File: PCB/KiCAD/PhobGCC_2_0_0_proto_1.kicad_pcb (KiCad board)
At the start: 2 copper layers, 125.5 x 90.3 mm, 113 parts, among them J1 Conn_01x06_Female, J11 Conn_01x02, J14 Conn_01x06, J15 Conn_01x06, J2 Conn_01x02, J3 Conn_01x02, J4 Conn_01x01, J5 Rumble, J6 Conn_01x06, J8 USB_B_Micro, Q1 Q_NMOS_GSD, Q2 Q_PMOS_GDS, Q3 Q_NMOS_GSD, SW1 A, SW10 Dup, SW11 Dright, SW12 Ddown, SW2 B, SW3 X, SW4 Y, SW5 Start, SW6 L, SW7 R, SW8 Z, SW9 Dleft, U1 MCP3202, U10 DRV5055A3xDBZxQ1, U11 DRV5055A3xDBZxQ1, U12 USBLC6-2P6, U13 USBLC6-2P6, U2 Stickbox_Assembly_Main, U3 MCP3202, U4 DRV5055A3xDBZxQ1, U5 Stickbox_Assembly_CStick, U6 AMS1117-3.3, U7 W25Q128JVS, U8 RP2040, U9 DRV5055A3xDBZxQ1, Y1 Crystal_GND24

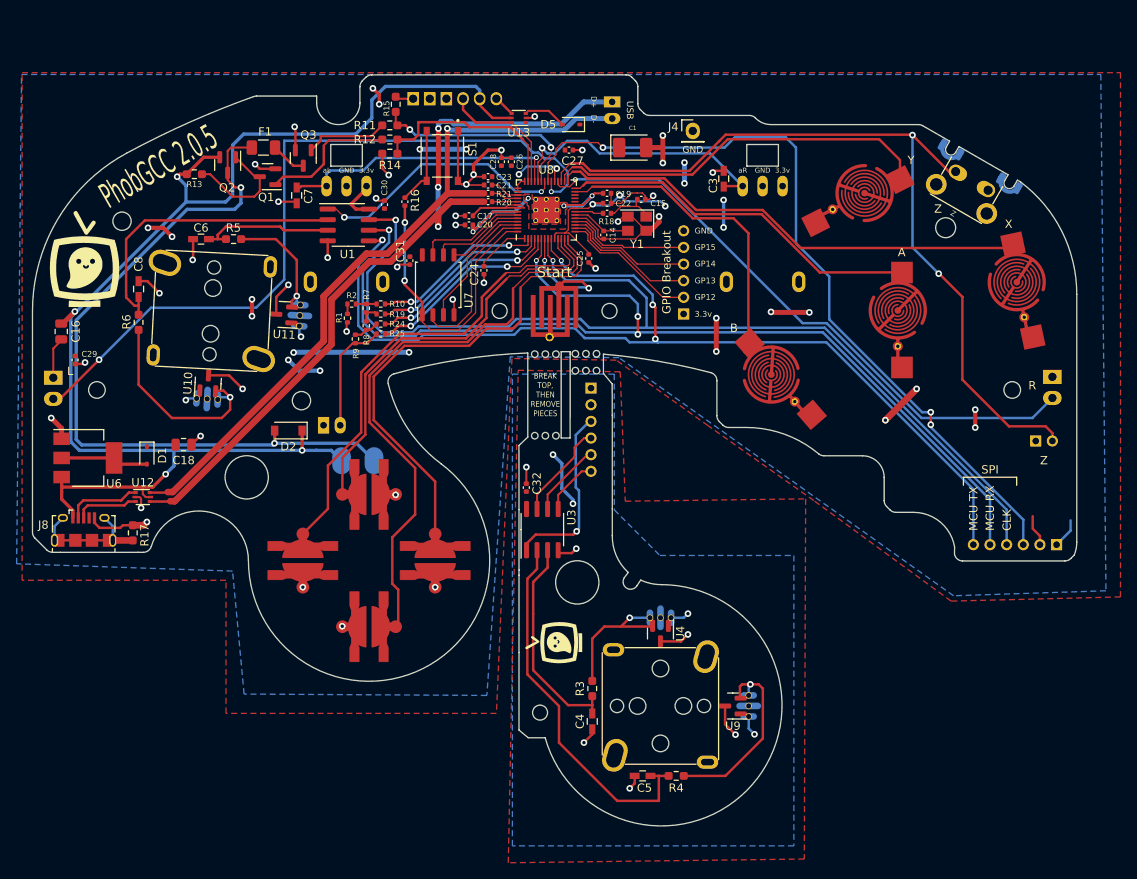
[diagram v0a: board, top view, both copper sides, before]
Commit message: NaxGCC Changes:
- update to KiCad 8
- replace micro USB & GCC connector with USB C
- add some JLCPCB symbols, footprints & models
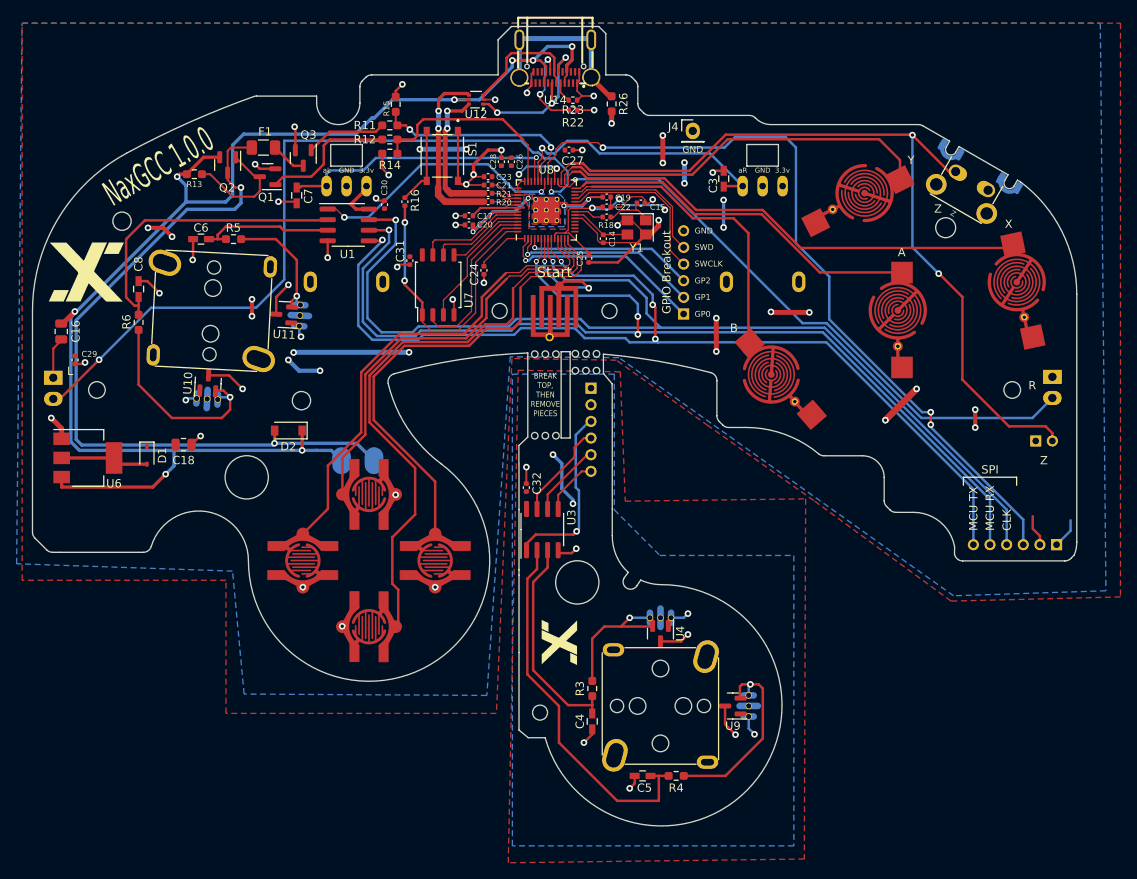
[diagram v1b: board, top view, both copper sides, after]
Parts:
- removed C1: 47u, Capacitor_Tantalum_SMD:CP_EIA-3528-12_Kemet-T_Pad1.50x2.35mm_HandSolder
- removed D5: CUS10S30,H3F, Diode_SMD:D_SOD-323
- removed Gphobtvbigback (x2): LOGO, Library:phobtv_bold_big
- removed Gtvsmallfrontc: LOGO, Library:phobtv_bold_smol
- removed J1: Conn_01x06_Female, PhobGCC_2_0_0_footprints:GCC_Header_Straight_1x06_Pitch2.00mm
- removed J11, J2: Conn_01x02, PhobGCC_2_0_0_footprints:PinHeader_1x02_P2.00mm_Vertical
- removed J8: USB_B_Micro, PhobGCC_2_0_0_footprints:USB_Micro-B_Amphenol_10118194_Horizontal
- removed R1, R2, R7, R8, R9: 180, PhobGCC_2_0_0_footprints:R_0402_1005Metric
- removed R10, R19, R24, R25: 316, PhobGCC_2_0_0_footprints:R_0402_1005Metric
- removed R17: 100k, Resistor_SMD:R_0603_1608Metric_Pad0.98x0.95mm_HandSolder
- removed U13: USBLC6-2P6, Package_TO_SOT_SMD:SOT-666
- added R22: 5.1k, Resistor_SMD:R_0402_1005Metric, F.Cu at (113.2, 27.0)
- added R23: 5.1k, Resistor_SMD:R_0402_1005Metric, F.Cu at (113.2, 25.8)
- added R26: 100k, Resistor_SMD:R_0603_1608Metric_Pad0.98x0.95mm_HandSolder, F.Cu at (117.8, 26.2)
- added U14: GT-USB-7013, footprint:USB-C-SMD_GT-USB-7013, F.Cu at (111.1, 21.1)
- SW10, SW11, SW12, SW9: footprint PhobGCC_2_0_0_footprints:Dpad_Contact_TL3315NF_2 -> PhobGCC_2_0_0_footprints:Dpad_Contact_TL3315NF_2_ZigZag
- moved U12 62.3 mm to (101.5, 25.7), turned to 180 degrees
- moved C14 0.45 mm to (116.8, 42.5)
- moved Y1 0.45 mm to (120.8, 41.1)
- moved C19 0.45 mm to (117.2, 37.5)
- moved R18 0.45 mm to (117.2, 39.9)
- moved C15 0.45 mm to (121.4, 38.2)
- moved C22 0.45 mm to (117.2, 38.6)
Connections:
- J6 pad 1: +3V3 -> /GP0
- J6 pad 2: /GPIO12 -> /GP1
- J6 pad 3: /GPIO13 -> /GP2
- J6 pad 4: /GPIO14 -> /SWCLK
- J6 pad 5: /GPIO15 -> /SWD
- U8 pad 15: /GPIO12 -> unconnected-(U8-GPIO12-Pad15)
- U8 pad 16: /GPIO13 -> unconnected-(U8-GPIO13-Pad16)
- U8 pad 17: /GPIO14 -> unconnected-(U8-GPIO14-Pad17)
- U8 pad 18: /GPIO15 -> unconnected-(U8-GPIO15-Pad18)
- U8 pad 2: /Ladder1 -> /GP0
- U8 pad 3: /Ladder2 -> /GP1
- U8 pad 4: /Ladder3 -> /GP2
- U8 pad 40: /GCC_DATA -> unconnected-(U8-GPIO28_ADC2-Pad40)
- U8 pad 5: /Ladder4 -> unconnected-(U8-GPIO3-Pad5)
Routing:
- net /USB_D+: track 94.3 -> 21.4 mm, vias 3 -> 2
- net /USB_D-: track 86.5 -> 17.2 mm, vias 1 -> 2
- net /GP0: track 0.00 -> 25.0 mm, vias 0 -> 1
- net /GP1: track 0.00 -> 24.3 mm, vias 0 -> 1
- net /Ladder4: track 23.9 -> 0.00 mm, vias 2 -> 0
- net /Ladder3: track 22.9 -> 0.00 mm, vias 2 -> 0
- net /Ladder2: track 21.9 -> 0.00 mm, vias 2 -> 0
- net /SHIELD: track 0.00 -> 21.0 mm
- net /Ladder1: track 20.9 -> 0.00 mm, vias 2 -> 0
- net /GP2: track 0.00 -> 20.6 mm, vias 0 -> 1
- net /SWCLK: track 0.00 -> 20.1 mm
- net /SWD: track 0.00 -> 18.4 mm
- net /GPIO12: track 17.0 -> 0.00 mm
- net /GPIO13: track 16.3 -> 0.00 mm
- net /GCC_DATA: track 15.9 -> 0.00 mm
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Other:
- board size 125.5 x 90.3 mm -> 125.5 x 96.1 mm
- board text added: "GP0"
- board text added: "GP1"
- board text added: "GP2"
- board text added: "NaxGCC 1.0.0"
- board text added: "SWCLK"
- board text added: "SWD"
- board text added: "github.com/Naxdy/NaxGCC-HW"
- board text removed: "5v"
- board text removed: "BLUE WIRE ON LEFT FOR OEM CABLES"
- board text removed: "D+"
- board text removed: "D-"
- board text removed: "Data"
- board text removed: "GP12"
- board text removed: "GP13"
- board text removed: "GP14"
- board text removed: "GP15"
- board text removed: "PhobGCC 2.0.5"
- board text removed: "PhobVision"
- board text removed: "USB"
- board text removed: "github.com/PhobGCC"
